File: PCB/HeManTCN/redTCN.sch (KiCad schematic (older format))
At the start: 1 part

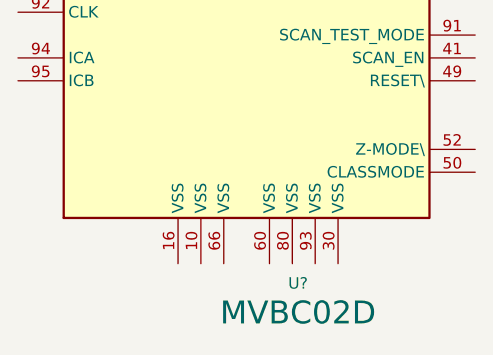
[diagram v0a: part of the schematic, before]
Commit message: Hoja A1
Desarme las hojas jerarquicas y configure la hoja del esquematico como A1. Hay lugar suficiente (por ahora) para todo.
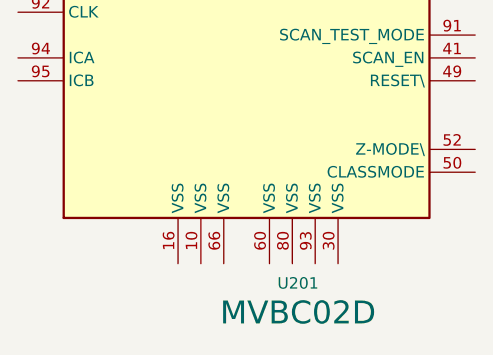
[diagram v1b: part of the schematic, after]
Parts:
- gave numbers to parts that had none: 1
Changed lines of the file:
@@
 $EndDescr
 $Comp
-L Bombardier:MVBC02D U?
+L Bombardier:MVBC02D U201
 U 1 1 5DA2AA78
 P 2450 3650
-F 0 "U?" H 2675 664 50  0000 C CNN
+F 0 "U201" H 2675 664 50  0000 C CNN
 F 1 "MVBC02D" H 2675 535 100 0000 C CNN
 F 2 "Package_QFP:QFP-100_14x20mm_P0.5mm" H 1650 950 50  0001 R CNN
